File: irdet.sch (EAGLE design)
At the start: 68 parts, among them IC1 MEGA8-AI, IC2 78L05F, J1 PSH02-04WG, J2 PSH02-04WG, J3 PSH02-04WG, J4 PSH02-04WG, J5 22-05-7098-09, T1 BC847, T2 BC857, T3 BC847, T4 BC857, T5 BC847, T6 BC857, T7 BC847, T8 BC857, X1 MVE252-5-V, X2 MVE252-5-V

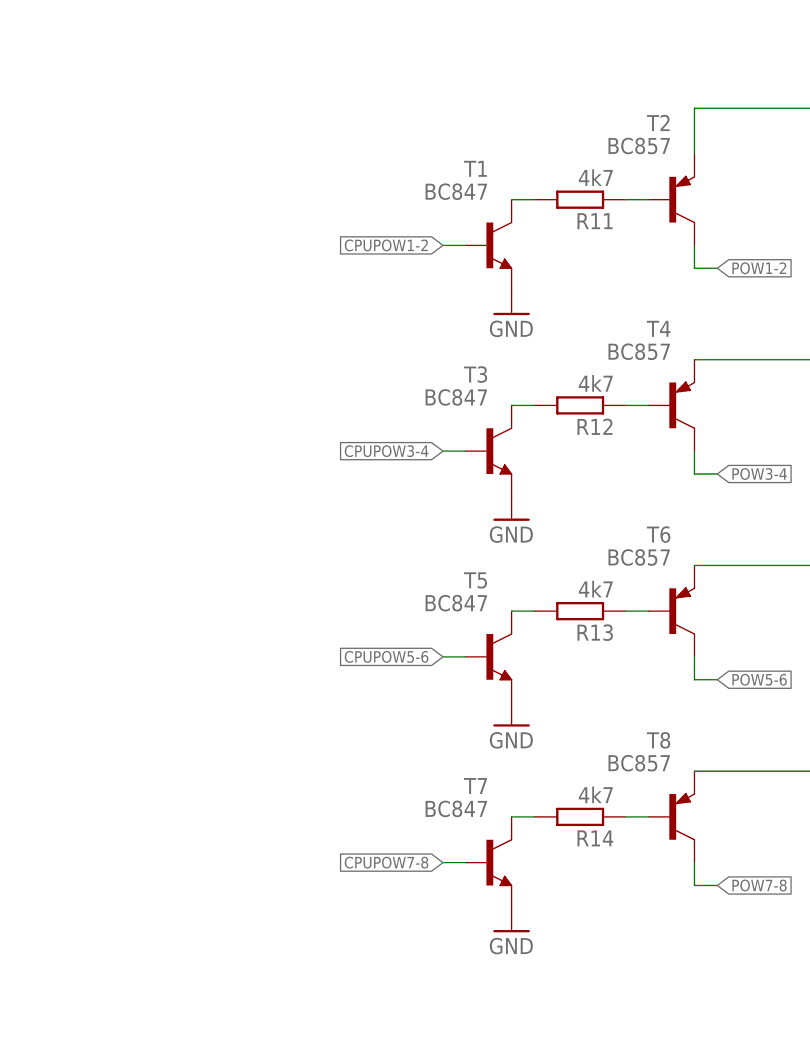
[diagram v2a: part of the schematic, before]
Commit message: Add resistors to transistor's base.
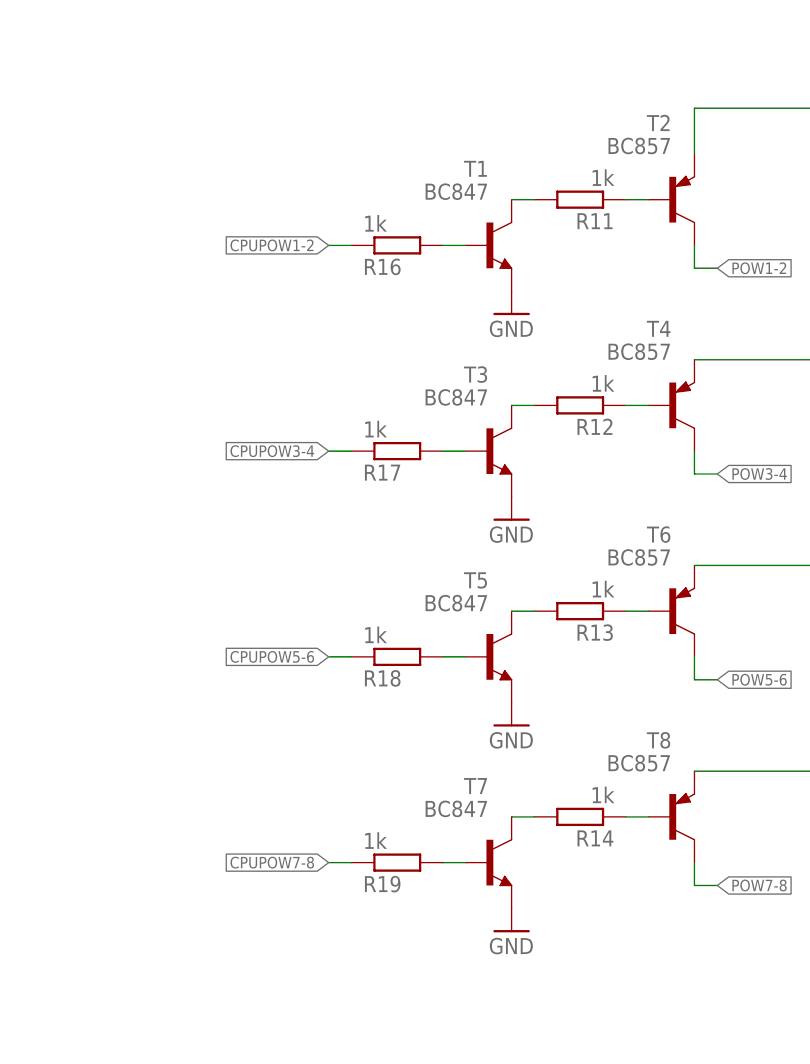
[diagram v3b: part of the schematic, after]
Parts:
- added R16, R17, R18, R19: 1k, rcl:R-EU_R0805
- R11, R12, R13, R14: value 4k7 -> 1k; LCSC_PART (none) -> C17513
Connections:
- new net N$48: R17.2, T3.B
- new net N$49: R16.2, T1.B
- new net N$50: R18.2, T5.B
- new net N$51: R19.2, T7.B
- net CPUPOW1-2: now also R16.1; no longer T1.B
- net CPUPOW3-4: now also R17.1; no longer T3.B
- net CPUPOW5-6: now also R18.1; no longer T5.B
- net CPUPOW7-8: now also R19.1; no longer T7.B

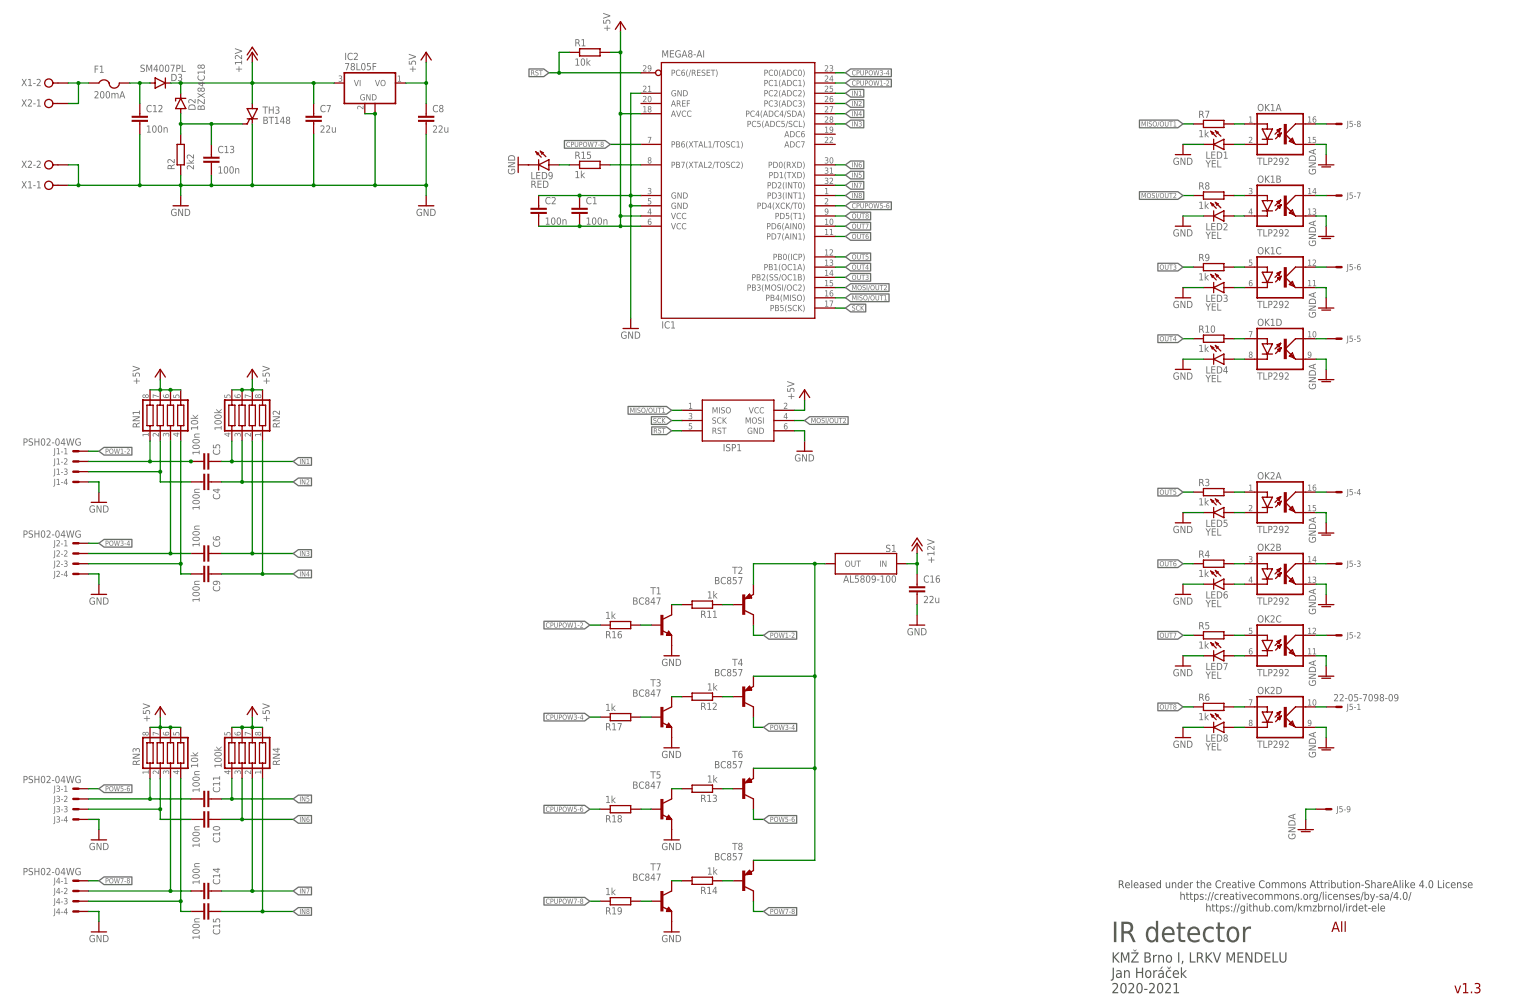
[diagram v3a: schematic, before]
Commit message: Update IR diode power.
* Add stabilizer to 8V + big resistor for current ~200 mA.
* Remove overvoltage protection.
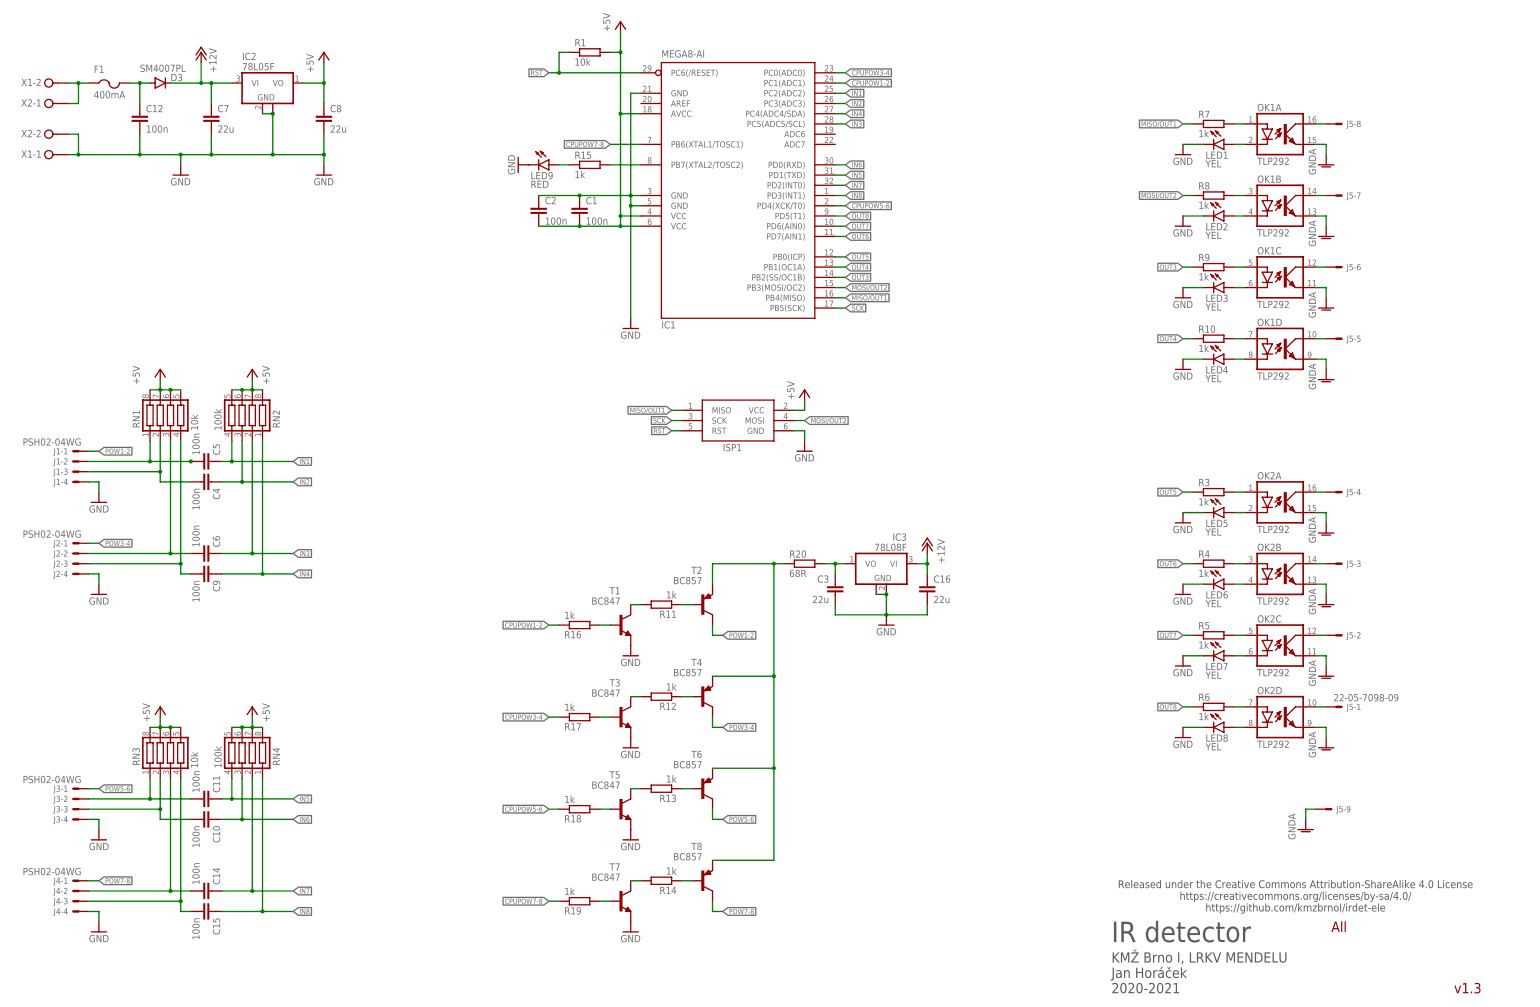
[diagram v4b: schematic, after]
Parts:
- removed C13: 100n, rcl:C-EUC0805
- removed D2: BZX84C18, diode:ZENER-DIODESOT23
- removed R2: 2k2, rcl:R-EU_R0805
- removed S1: AL5809-100, current-stabilizers:AL5809
- removed TH3: BT148, ElectroKrt:BT148
- added C3: 22u, rcl:C-EUC0805
- added IC3: 78L08F, linear:78L08F
- added R20: 68R, rcl:R-EU_R2010
- F1: value 200mA -> 400mA
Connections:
- removed net N$57: C13.1, D2.A, R2.2, TH3.G
- new net +8V: C3.1, IC3.VO, R20.2
- net +12V: now also IC3.VI; no longer D2.C, S1.IN, TH3.A
- net GND: now also C3.2, IC3.GND, IC3.GND@1; no longer C13.2, R2.1, TH3.C
- net N$42: now also R20.1; no longer S1.OUT
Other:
- moved on the sheet: C16, C7, C8, IC2, R11, R12, R13, R14, R16, R17, R18, R19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

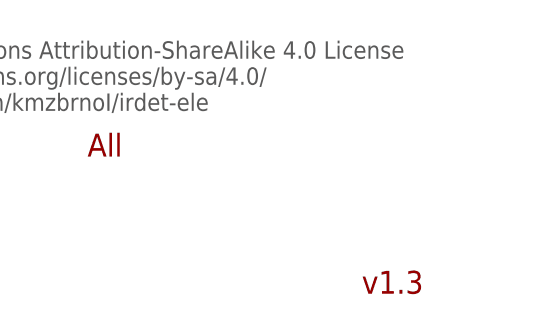
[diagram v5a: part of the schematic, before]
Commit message: Change version to 2.0.
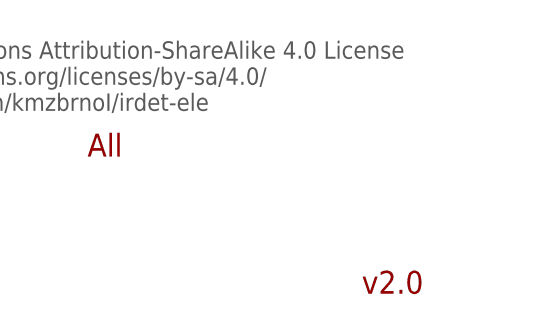
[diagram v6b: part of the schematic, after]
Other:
- note added: "v2.0"
- note removed: "v1.3"
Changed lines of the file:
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@@
 <plain>
 <text x="289.56" y="17.78" size="5.08" layer="97">IR detector</text>
-<text x="374.65" y="5.08" size="2.54" layer="94">v1.3</text>
+<text x="374.65" y="5.08" size="2.54" layer="94">v2.0</text>
 <text x="289.56" y="5.08" size="2.54" layer="97">KMŽ Brno I, LRKV MENDELU
 Jan Horáček

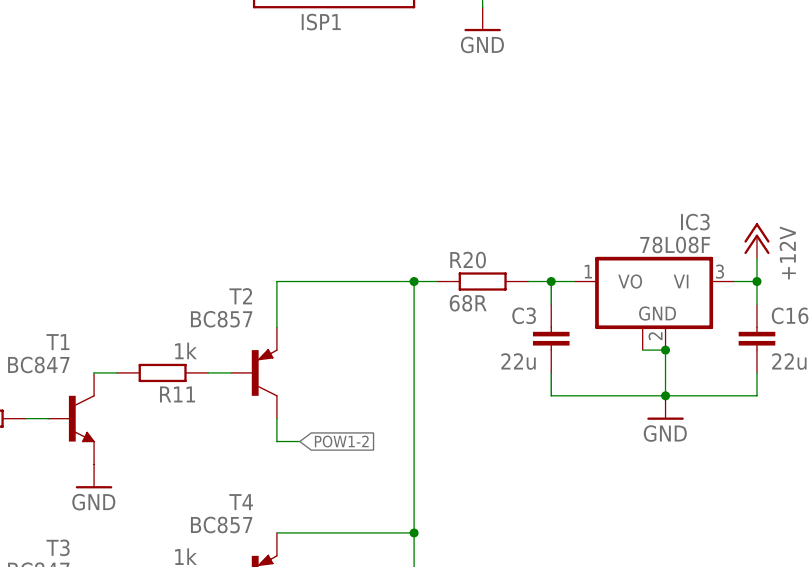
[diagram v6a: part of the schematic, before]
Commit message: Make silkscreen nice.
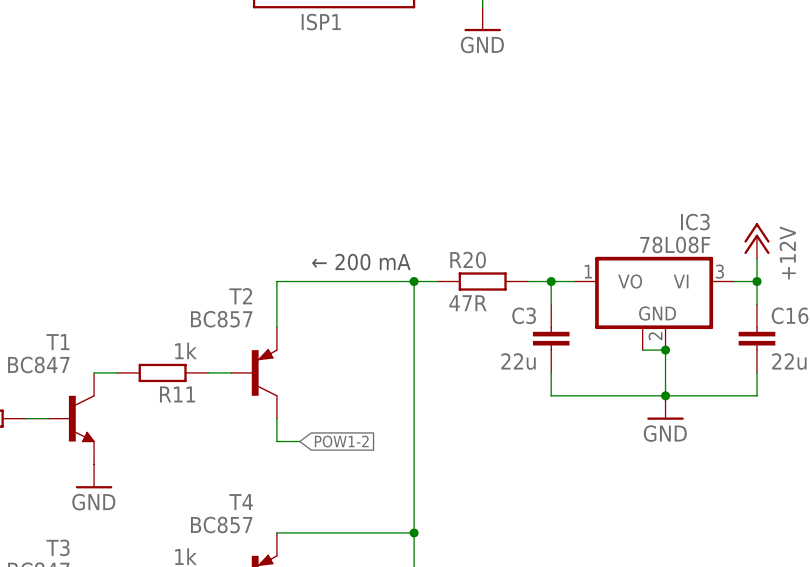
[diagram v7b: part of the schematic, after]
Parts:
- R20: value 68R -> 47R
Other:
- note added: "← 200 mA"
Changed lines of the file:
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@@
 </part>
 <part name="GND30" library="supply1" library_urn="urn:adsk.eagle:library:371" deviceset="GND" device=""/>
-<part name="R20" library="rcl" library_urn="urn:adsk.eagle:library:334" deviceset="R-EU_" device="R2010" package3d_urn="urn:adsk.eagle:package:23551/2" value="68R"/>
+<part name="R20" library="rcl" library_urn="urn:adsk.eagle:library:334" deviceset="R-EU_" device="R2010" package3d_urn="urn:adsk.eagle:package:23551/2" value="47R"/>
 </parts>
 <sheets>
@@
 https://github.com/kmzbrnoI/irdet-ele</text>
 <text x="344.17" y="20.32" size="2.54" layer="94">All</text>
+<text x="194.31" y="113.03" size="1.778" layer="97">← 200 mA</text>
 </plain>
 <instances>
